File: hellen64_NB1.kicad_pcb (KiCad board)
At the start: 2 copper layers, 154 x 161.5 mm, 168 parts, among them J1 USB_B_Mini, J11 Conn_01x01, J12 Conn_01x01, J13 Conn_01x01, J14 Conn_01x01, J15 Conn_01x01, J16 Conn_01x01, J17 Conn_01x01, J18 Conn_01x01, J19 Conn_01x01, J2 Conn_01x05_Male, J20 Conn_01x01, J21 Conn_01x01, J22 Conn_01x01, J24 Conn_01x01, J25 AudioJack3_SwitchTR, J27 Conn_01x06, J3 Conn_01x06, J4 Conn_02x12_Odd_Even, J5 USB_B, M1 Module-input-0.1, M10 Module-power12-0.2, M11 Module-power5-0.2, M12 Module-wbo-0.2, M13 Module-can-0.1, M2 Module-ign8-0.1, M3 Module-mcu-0.3, M4 Module-sd-0.1, M5 Module-output-0.2, M6 Module-dinput4-0.1, M7 Module-stlink-0.1, M8 Module-can-0.1, M9 Module-knock-0.1, P1 Pad, P10 Pad, P11 Pad, P12 Pad, P13 Pad, P14 Pad, P15 Pad, P17 Pad, P18 Pad, P2 176122-6_2nd, P20 Pad, P22 Pad, P23 Pad, P24 Pad, P25 Pad, P26 Pad, P27 Pad, P28 Pad, P29 Pad, P3 Pad, P30 Pad, P31 Pad, P32 Pad, P34 Pad, P38 Pad, P4 Pad, P40 Pad, P43 Pad, P44 Pad, P46 Pad, P47 Pad, P48 Pad, P49 Pad, P5 Pad, P50 Pad, P51 Pad, P52 Pad, P53 Pad, P55 Pad, P56 Pad, P6 Pad, P7 Pad, P9 Pad, U1 LIS2DW12TR, U2 MPX4_MAP, U3 MCP6002-xSN, U4 LPS25HB

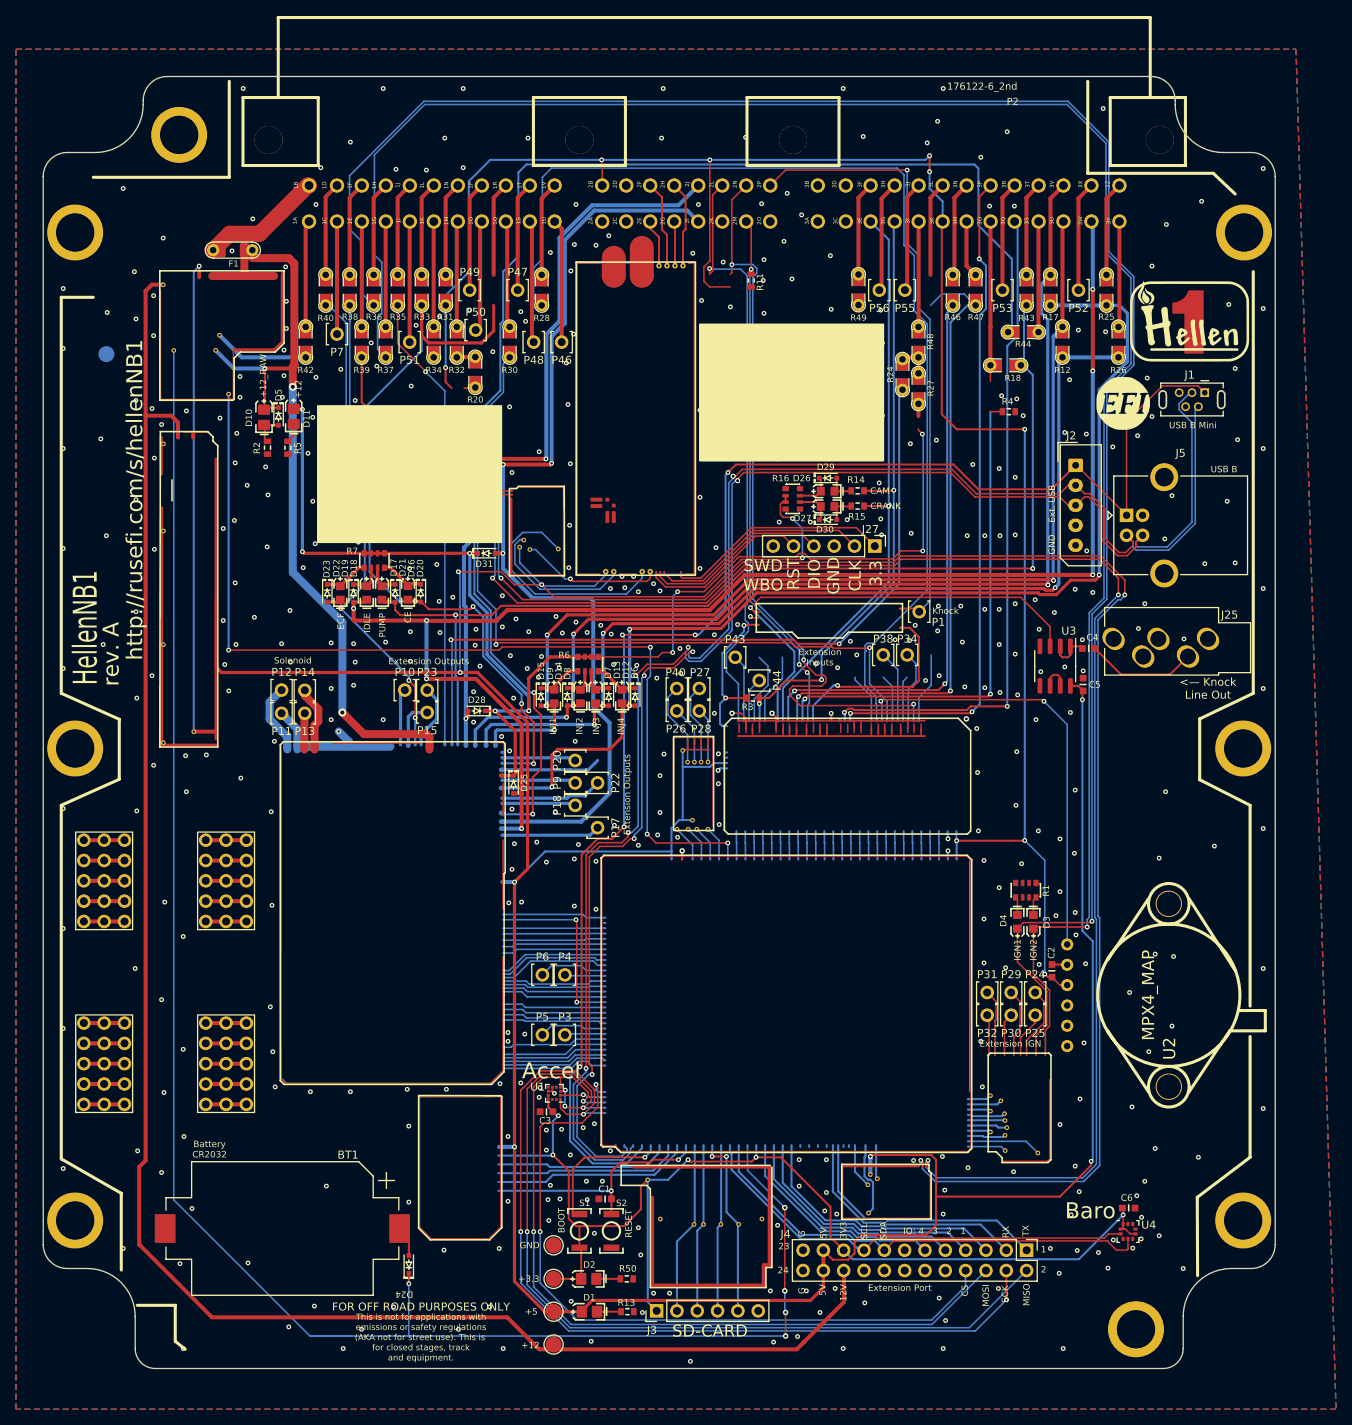
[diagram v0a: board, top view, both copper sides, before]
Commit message: new pcb board shape, dims & holes for NB1 + trying to fit components inside (remove SD-card ext.header)
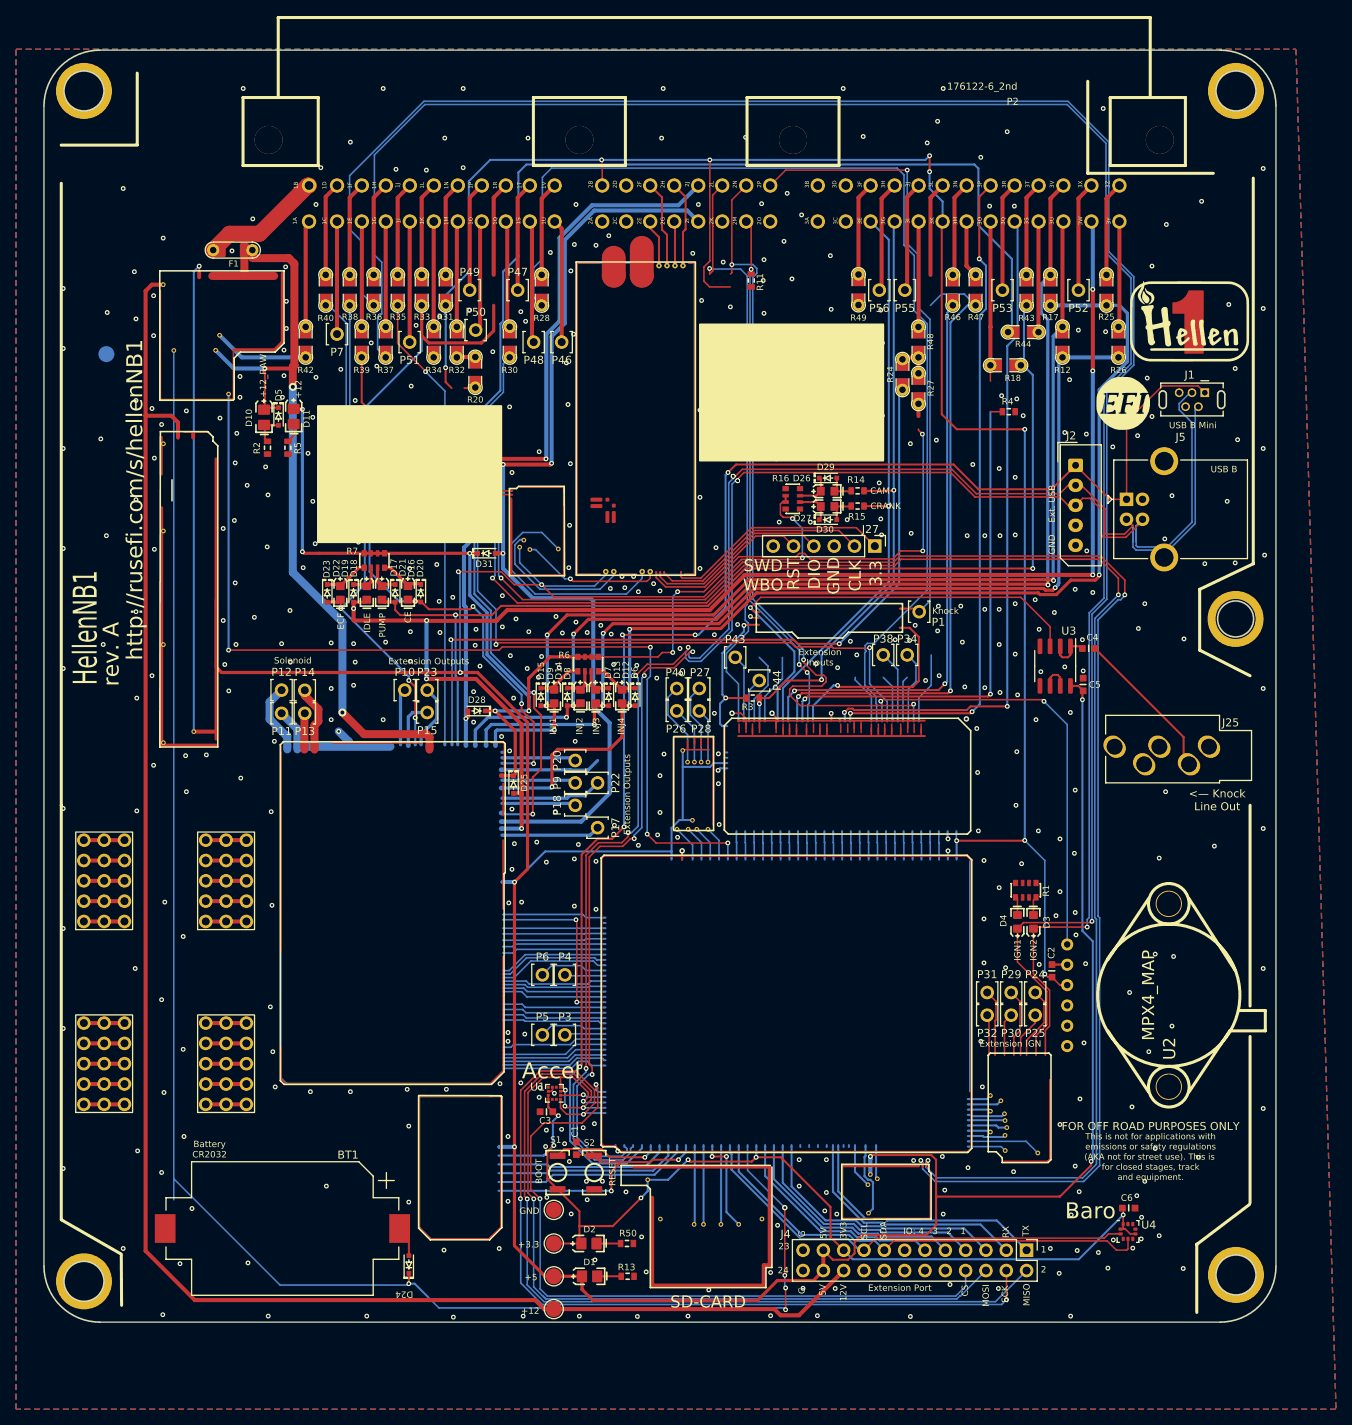
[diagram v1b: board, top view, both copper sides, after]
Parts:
- removed J12, J17, J18: Conn_01x01, MountingHole:MountingHole_4.5mm_Pad
- removed J3: Conn_01x06, Connector_PinHeader_2.54mm:PinHeader_1x06_P2.54mm_Vertical
- moved J16 17.7 mm to (170.1, 16.8)
- moved J15 16.2 mm to (170.0, 82.8)
- moved J25 13.5 mm to (162.9, 99.1)
- moved J11 13.1 mm to (26.1, 16.8)
- moved S1 7.79 mm to (85.3, 152.0)
- moved J13 7.68 mm to (26.1, 165.6)
- moved S2 7.61 mm to (89.9, 152.0)
- moved C1 7.27 mm to (87.7, 149.0), turned to -90 degrees
- moved J14 6.86 mm to (170.1, 164.8)
- moved D1 4.43 mm to (89.3, 165.0)
- moved D2 4.43 mm to (89.2, 160.9)
- moved J19 4.43 mm to (84.8, 169.1)
- moved J20 4.43 mm to (84.8, 165.0)
- moved J21 4.43 mm to (84.8, 160.9)
- moved R13 4.43 mm to (94.1, 165.0)
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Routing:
- net /IN_STEERING: track 256.7 -> 8.82 mm, vias 1 -> 0
- net /OUT_IGN1: track 79.2 -> 327.1 mm, vias 2 -> 3
- net /OUT_IGN2: track 1.54 -> 248.5 mm, vias 0 -> 1
- net /OUT_AC_FAN_RELAY: track 247.0 -> 0.00 mm, vias 1 -> 0
- net /CAN-: track 57.3 -> 294.0 mm, vias 1 -> 6
- net /IN_BRAKE: track 242.3 -> 5.60 mm, vias 5 -> 0
- net /USB-: track 191.9 -> 393.3 mm, vias 6 -> 12
- net /USB+: track 196.8 -> 0.00 mm, vias 6 -> 0
- net /IN_AFR: track 0.00 -> 100.8 mm, vias 0 -> 3
- net /2N: track 95.2 -> 6.96 mm, vias 3 -> 0
- net /IN_O2S2: track 96.9 -> 172.0 mm, vias 2 -> 3
- net /IN_MAF: track 138.2 -> 63.1 mm, vias 3 -> 2
- net +3V3: track 142.0 -> 122.8 mm, vias 5 -> 6
- net /1U: track 13.2 -> 28.7 mm
- net /1Q: track 15.4 -> 0.00 mm
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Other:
- board size 154 x 161.5 mm -> 154 x 159 mm

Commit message: New 178780-1 76p connector footprint & board holes
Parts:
- added J17: Conn_01x01, MountingHole:MountingHole_4.5mm_Pad, F.Cu at (26.1, 98.8)
- P2: value 176122-6_2nd -> 178780-1; footprint rusefi_lib:176122-6_2nd -> hellen-one-common:178780-1
- moved P2 17.1 mm to (146.6, 33.1)
- moved J15 16.0 mm to (170.0, 98.8)
- moved J25 16.0 mm to (162.9, 83.1)
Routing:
- net /1U: track 28.7 -> 13.2 mm
- net /1Q: track 0.00 -> 15.4 mm
- net Net-(P2-Pad21): track 0.00 -> 13.9 mm
- net /3H: track 18.0 -> 4.09 mm
- net /3L: track 11.8 -> 0.00 mm
- net /3J: track 0.00 -> 11.8 mm
- net /IN_KNOCK_RAW: track 88.2 -> 77.3 mm
- net /WBO_Ip: track 0.00 -> 10.9 mm
- net /IN_CAM: track 87.1 -> 76.4 mm
- net /WBO_Vs: track 0.00 -> 10.7 mm
- net /IN_AFR: track 100.8 -> 95.2 mm
- net /WBO_Vs/Ip: track 0.00 -> 5.56 mm
- net Net-(C4-Pad1): track 19.1 -> 14.4 mm
- net GND: vias 479 -> 477
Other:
- outline, holes or cut-outs redrawn

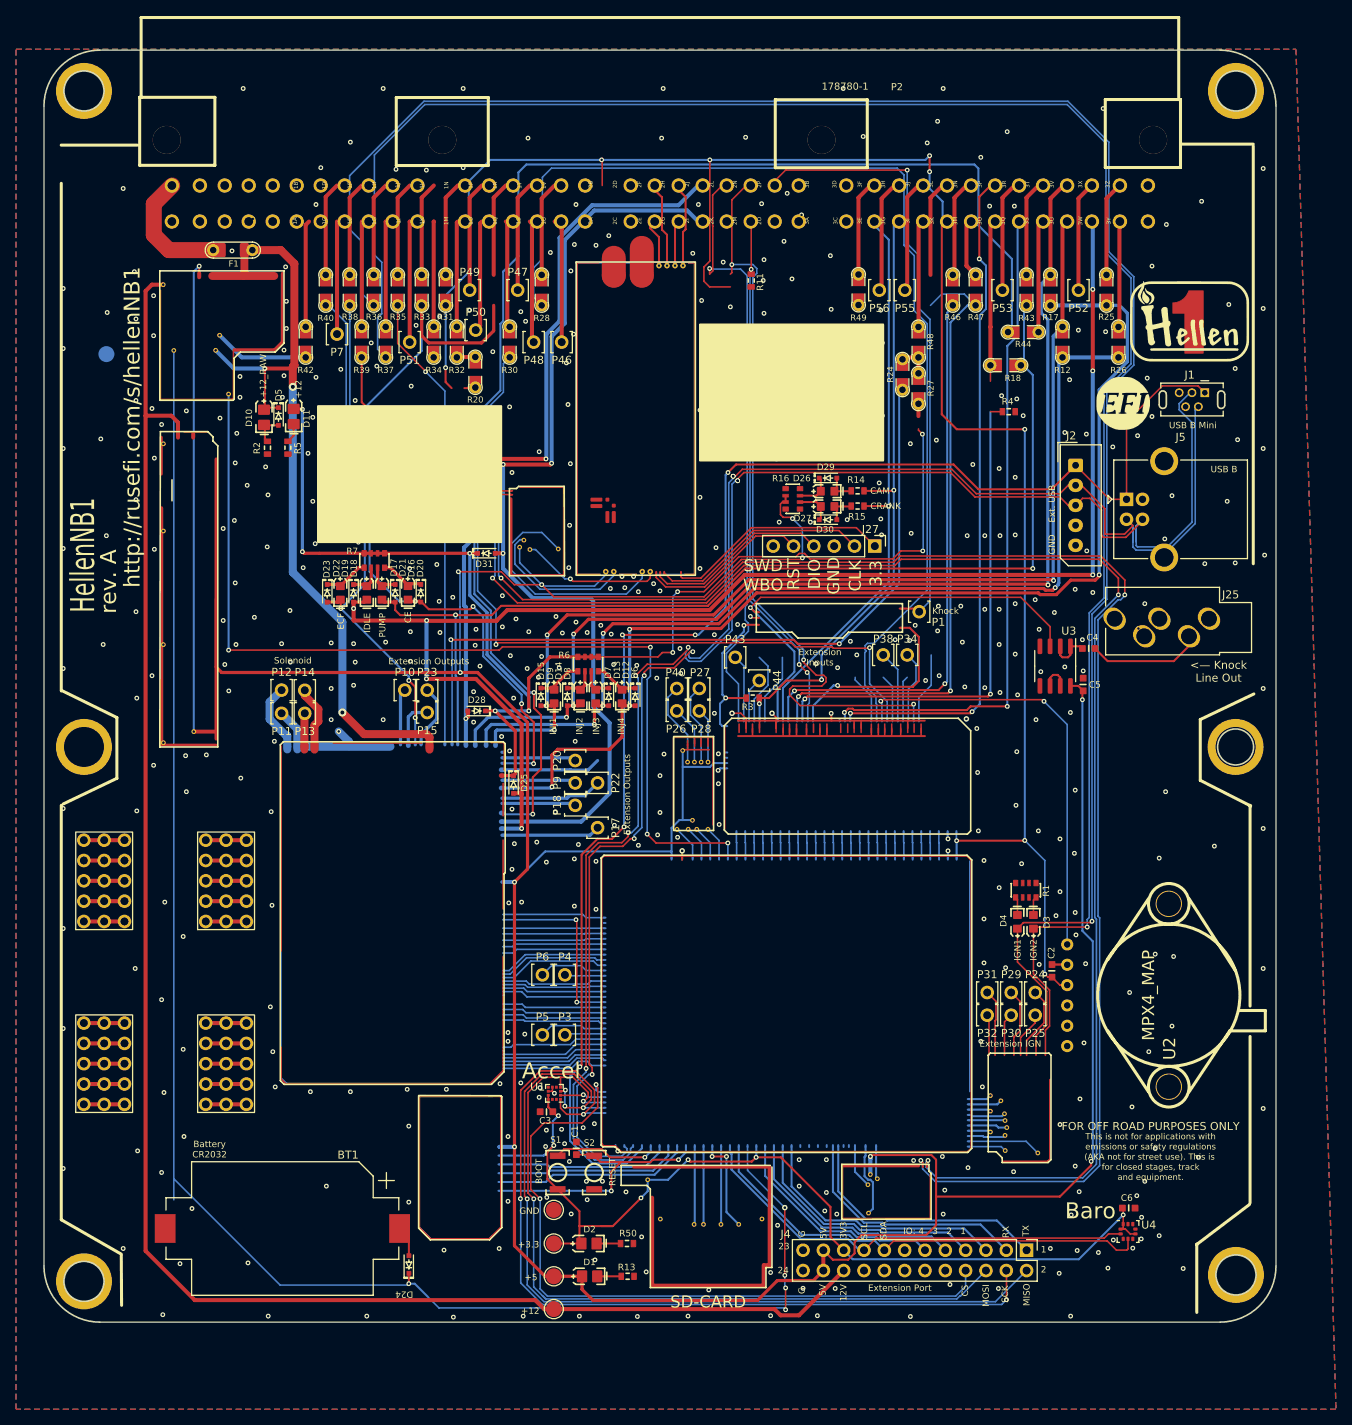
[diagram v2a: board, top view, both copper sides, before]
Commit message: update schematic
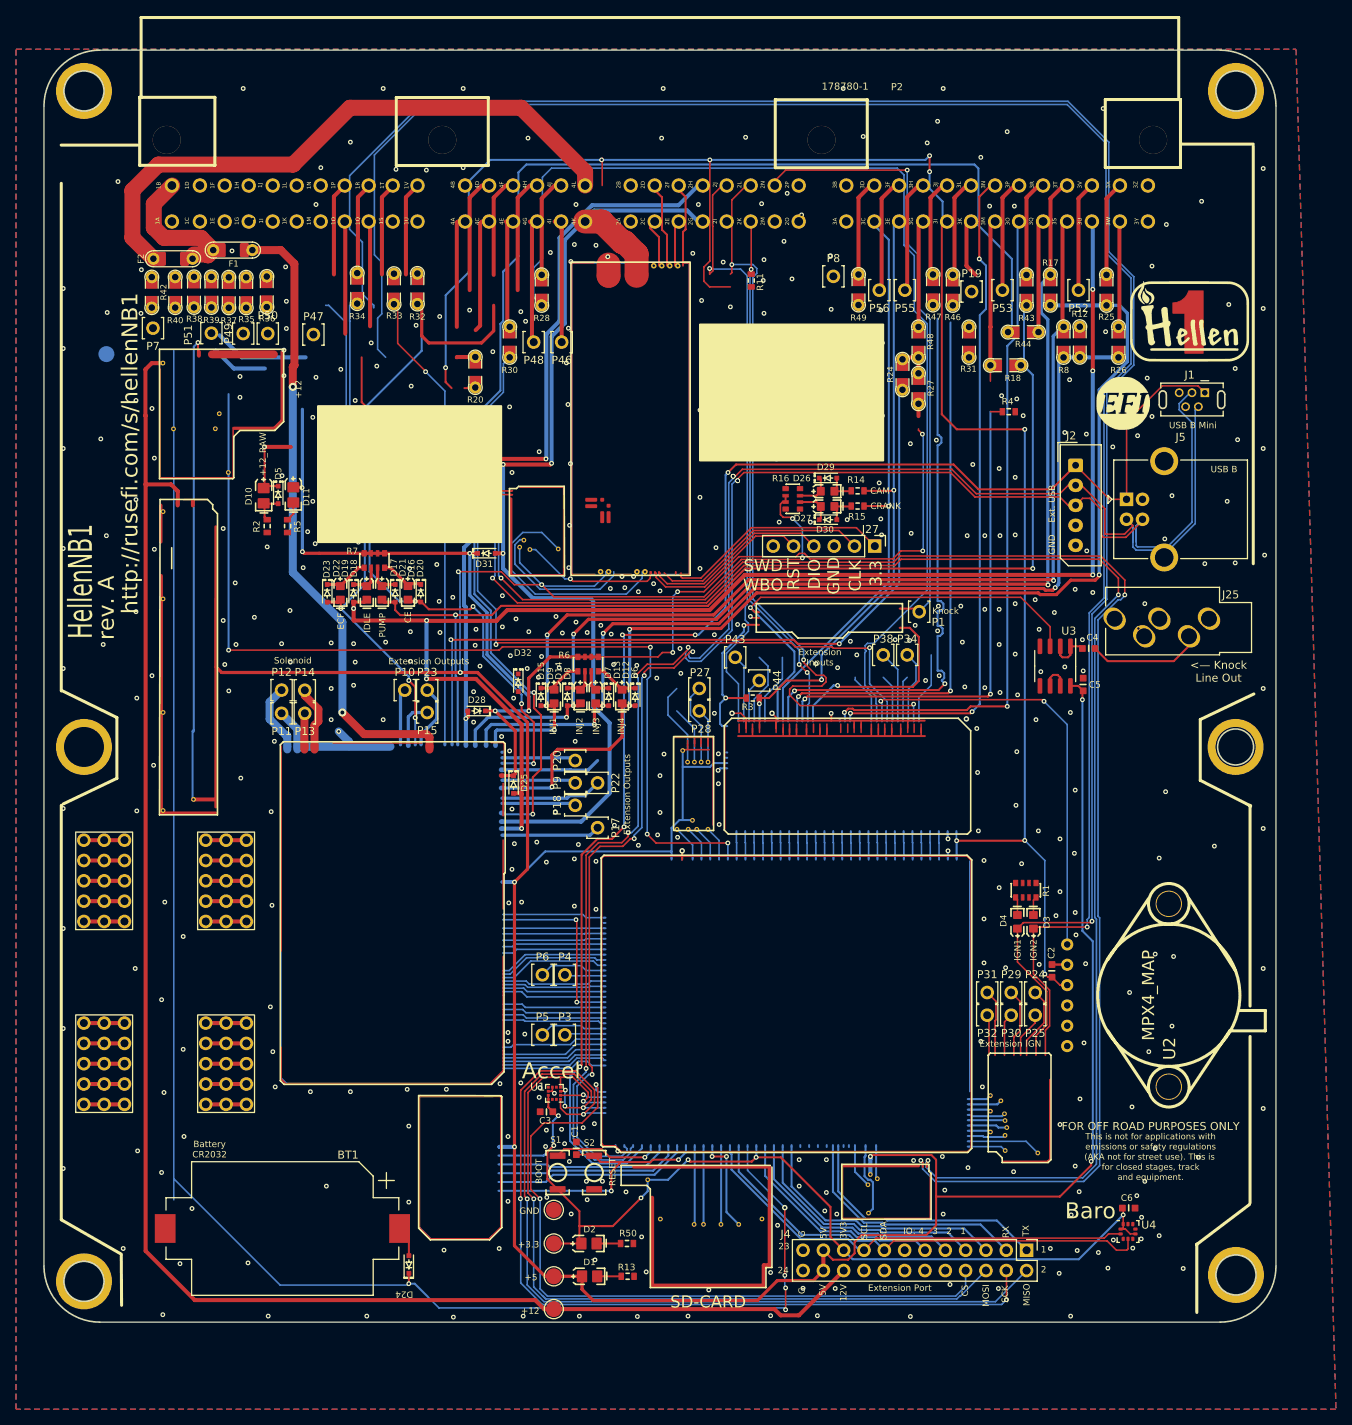
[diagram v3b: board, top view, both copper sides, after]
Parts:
- removed P26, P40: Pad, hellen-one-common:PAD-TH
- added D32: 1N4148WS, hellen-one-common:SOD-323, F.Cu at (80.4, 90.8)
- added F2: Fuse-Pad-Pad, hellen-one-common:PAD-1206-PAD, F.Cu at (37.2, 37.8)
- added P19: Pad, hellen-one-common:PAD-TH, F.Cu at (137.0, 41.9)
- added P8: Pad, hellen-one-common:PAD-TH, F.Cu at (119.8, 40.0)
- added R8: Jumper-Pad-Pad, hellen-one-common:PAD-0805-PAD, F.Cu at (148.5, 48.2)
- moved R31 65.7 mm to (136.7, 48.2)
- moved P49 28.8 mm to (46.0, 47.1)
- moved P47 26.1 mm to (54.8, 47.3)
- moved P50 26.0 mm to (49.1, 47.1)
- moved P51 24.8 mm to (42.0, 47.1)
- moved P7 23.0 mm to (34.7, 46.5)
- moved R37 20.6 mm to (44.2, 42.0)
- moved R42 20.2 mm to (34.6, 42.0)
- moved R39 19.8 mm to (42.0, 42.0)
- moved R38 19.5 mm to (39.8, 42.0)
- moved R35 18.9 mm to (46.4, 42.0)
- moved R40 18.8 mm to (37.5, 42.0)
- moved R36 13.4 mm to (48.9, 41.9)
- moved R34 11.7 mm to (60.2, 41.5)
- moved D10 9.80 mm to (48.6, 67.4)
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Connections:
- net /AUX1 renamed /PRESSURE
- net /AUX4 renamed /EGR_BOOST
- net /D1 renamed /DIGITAL
- net /O2S2 renamed /AFR
- net /OUT_EGR_BOOST renamed /OUT_BOOST
- net /RES1 renamed /BRAKE
- net /RES2 renamed /STEERING
- net /SENS4 renamed /NEUTRAL
- M1 pad N9: /CLUTCH -> /TEMP
- M1 pad S18: /IN_CLUTCH -> /IN_TEMP
- M3 pad S25: /CLUTCH -> /TEMP
- M3 pad S4: /D2 -> /CLUTCH
- M5 pad W1: unconnected-(M5-PadW1) -> /OUT_AC_FAN_RELAY
- M5 pad W10: /OUT_AC_FAN_RELAY -> /OUT_VVT
- M6 pad V2: /IN_D1 -> /IN_DIGITAL
- M6 pad V3: /IN_D2 -> /IN_CLUTCH
- M6 pad W3: /D2 -> /CLUTCH
- P2 pad 65: (no net) -> GND
- P2 pad 66: (no net) -> /IN_TEMP
- P2 pad 67: (no net) -> /OUT_VVT
- P2 pad 68: (no net) -> /WBO_Vs/Ip
- P2 pad 69: (no net) -> /WBO_R_Trim
- P2 pad 70: (no net) -> /WBO_H-
- P2 pad 71: (no net) -> /IN_DIGITAL
- P2 pad 72: (no net) -> Net-(P2-Pad72)
- P2 pad 73: (no net) -> +5VA
- P2 pad 74: (no net) -> /WBO_Vs
- P2 pad 75: (no net) -> /WBO_Ip
- P2 pad 76: (no net) -> /4L
- R43 pad 2: /3T -> Net-(P2-Pad72)
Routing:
- net /IN_CAM: track 76.4 -> 477.9 mm, vias 3 -> 5
- net /USB-: track 393.3 -> 0.00 mm, vias 12 -> 0
- net /USB+: track 0.00 -> 393.3 mm, vias 0 -> 12
- net /OUT_IGN2: track 248.5 -> 1.54 mm, vias 1 -> 0
- net /WBO_H-: track 3.48 -> 226.1 mm, vias 0 -> 6
- net /OUT_IGN1: track 327.1 -> 545.7 mm, vias 3 -> 2
- net /OUT_VICS: track 203.4 -> 0.00 mm, vias 5 -> 0
- net /IN_EGR_BOOST: track 176.9 -> 5.87 mm, vias 2 -> 0
- net /IN_NEUTRAL: track 145.8 -> 9.05 mm
- net +5VA: track 269.1 -> 378.2 mm, vias 11 -> 14
- net /IN_AFR: track 95.2 -> 0.00 mm, vias 3 -> 0
- net /OUT_BOOST: track 95.1 -> 0.00 mm, vias 3 -> 0
- net /3N: track 11.8 -> 95.4 mm, vias 0 -> 3
- net /IN_CLT: track 0.00 -> 83.1 mm, vias 0 -> 2
- net /4L: track 0.00 -> 75.5 mm
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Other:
- board text added: "4A"
- board text added: "4B"
- board text added: "4C"
- board text added: "4D"
- board text added: "4E"
- board text added: "4F"
- board text added: "4G"
- board text added: "4H"
- board text added: "4I"
- board text added: "4J"
- board text added: "4K"
- board text added: "4L"
